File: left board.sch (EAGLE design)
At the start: 29 parts, among them IC1 LM555D, IC2 LM555D

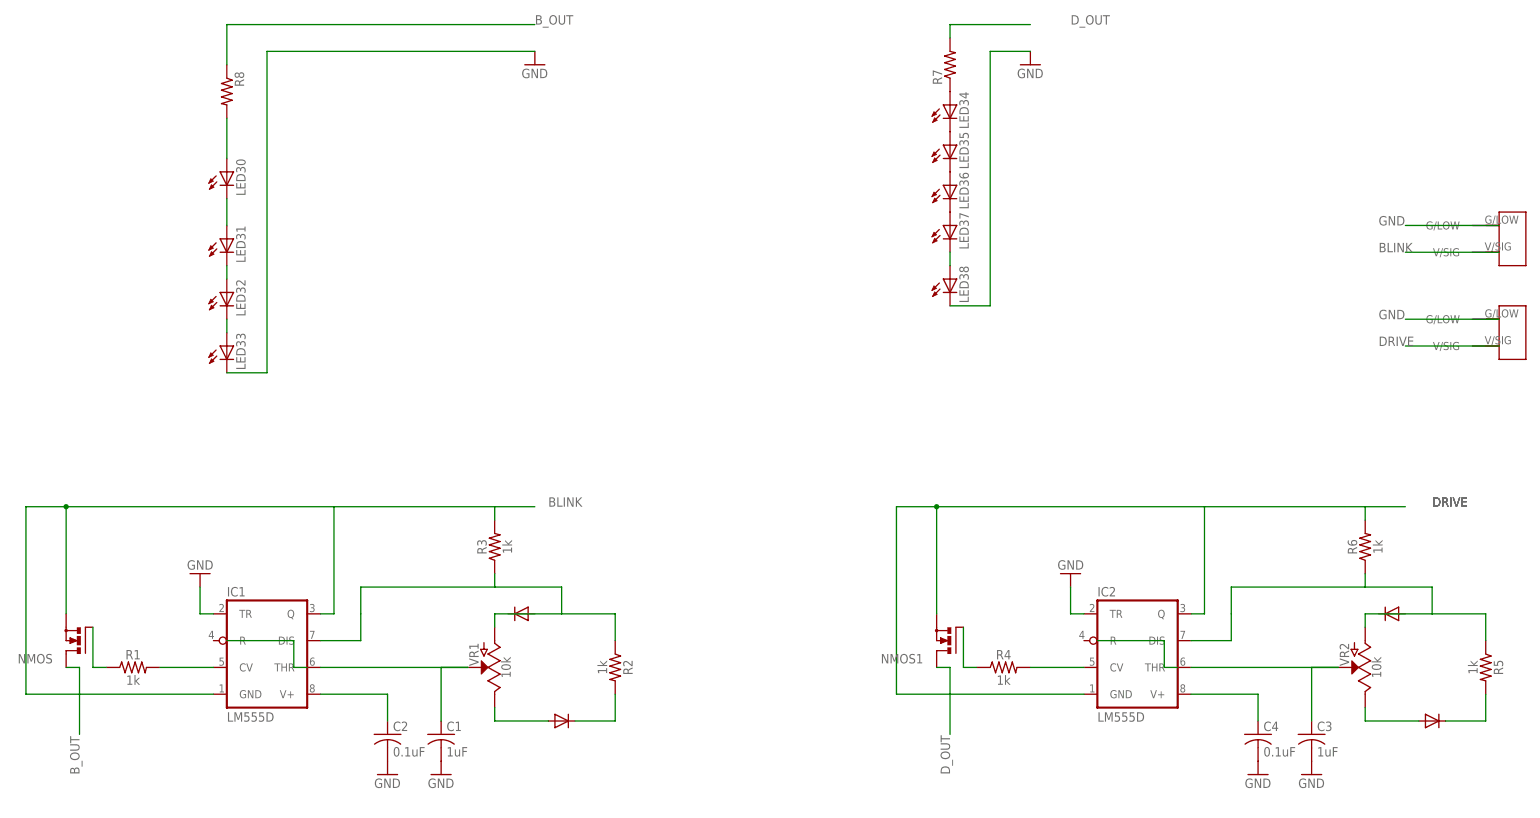
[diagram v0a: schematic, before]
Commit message: added switches to light board
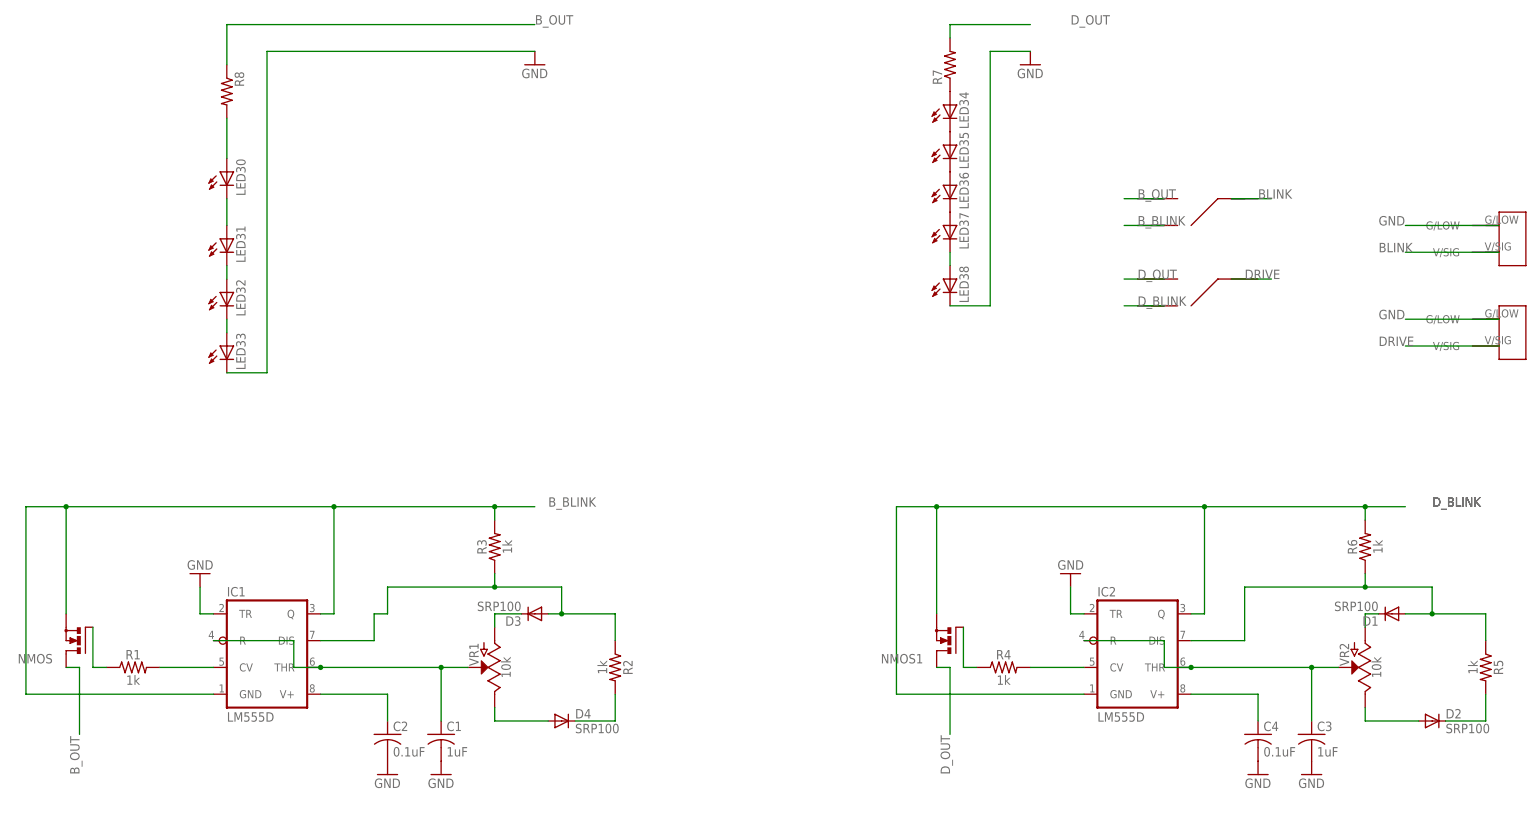
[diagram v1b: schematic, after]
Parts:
- added D1, D2, D3, D4: SRP100, diode:SRP100
- added U$1, U$2: JS_SERIES_SLIDESWITCCH, slide switch:JS_SERIES_SLIDESWITCCH
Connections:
- removed net N$12: IC2.DIS
- new net B_BLINK: IC1.GND, IC1.Q, NMOS.S, R3.2, U$1.OUT1
- new net D_BLINK: IC2.GND, IC2.Q, NMOS1.S, R6.2, U$2.OUT1
- new net N$9: D1.C, VR2.A
- net BLINK: now also U$1.IN; no longer IC1.GND, IC1.Q, NMOS.S, R3.2
- net B_OUT: now also U$1.OUT2
- net DRIVE: now also U$2.IN; no longer IC2.GND, IC2.Q, NMOS1.S, R6.2
- net D_OUT: now also U$2.OUT2
- net N$13: now also IC2.R
- net N$14: now also D1.A, IC2.DIS; no longer VR2.A
- net N$17: now also D2.A
- net N$18: now also D2.C
- net N$2: now also D3.C, VR1.A; no longer IC1.DIS
- net N$3: now also IC1.R
- net N$4: now also D3.A, IC1.DIS; no longer VR1.A
- net N$5: now also D4.A
- net N$7: now also D4.C

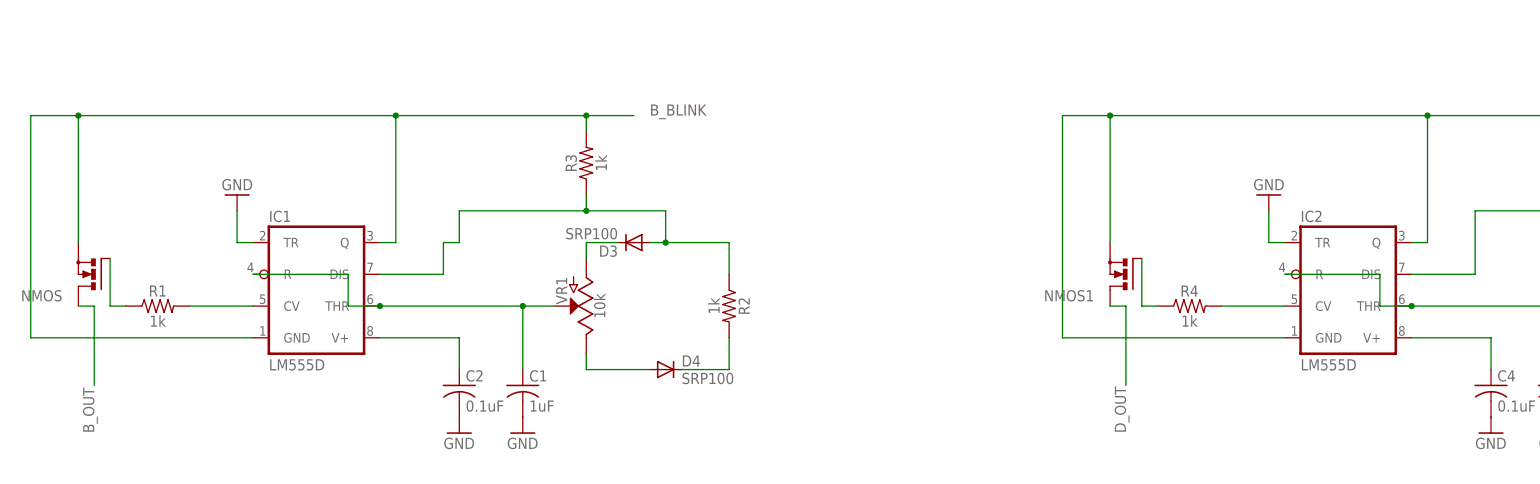
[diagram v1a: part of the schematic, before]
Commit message: updated for correct fets and routing
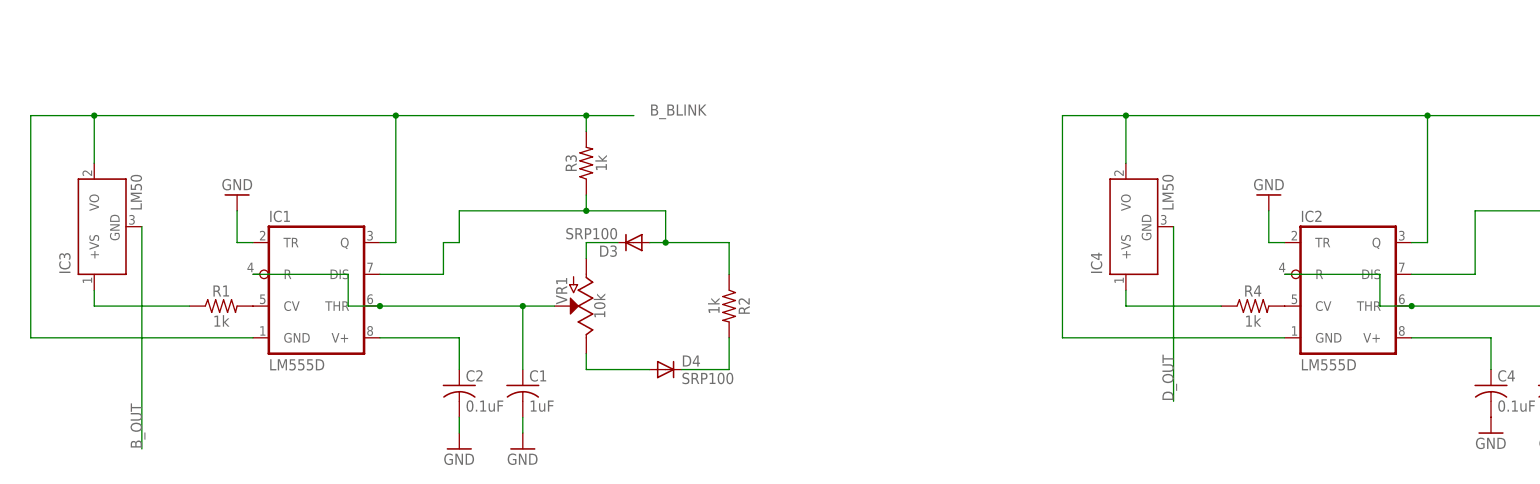
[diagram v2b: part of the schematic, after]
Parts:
- removed NMOS, NMOS1: (no value), transistor-power:N-MOSFET-SO8S
- added IC3, IC4: LM50, linear:LM50
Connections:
- removed net N$19: NMOS1.G, R4.1
- removed net N$8: NMOS.G, R1.1
- new net N$1: IC3.+VS, R1.1
- new net N$11: IC4.+VS, R4.1
- net B_BLINK: now also IC3.VO; no longer NMOS.S
- net B_OUT: now also IC3.GND; no longer NMOS.D
- net D_BLINK: now also IC4.VO; no longer NMOS1.S
- net D_OUT: now also IC4.GND; no longer NMOS1.D
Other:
- moved on the sheet: R1, R4
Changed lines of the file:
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@@
 <part name="C2" library="E-P-008-R1.2" deviceset="C-US" device="025-024X044" value="0.1uF"/>
 <part name="GND1" library="E-P-008-R1.2" deviceset="GND" device=""/>
-<part name="NMOS" library="transistor-power" library_urn="urn:adsk.eagle:library:400" deviceset="N-MOSFET-SO8" device="S" package3d_urn="urn:adsk.eagle:package:29505/2"/>
 <part name="GND2" library="E-P-008-R1.2" deviceset="GND" device=""/>
 <part name="GND4" library="E-P-008-R1.2" deviceset="GND" device=""/>
@@
 <part name="C4" library="E-P-008-R1.2" deviceset="C-US" device="025-024X044" value="0.1uF"/>
 <part name="GND5" library="E-P-008-R1.2" deviceset="GND" device=""/>
-<part name="NMOS1" library="transistor-power" library_urn="urn:adsk.eagle:library:400" deviceset="N-MOSFET-SO8" device="S" package3d_urn="urn:adsk.eagle:package:29505/2"/>
 <part name="GND6" library="E-P-008-R1.2" deviceset="GND" device=""/>
 <part name="GND8" library="E-P-008-R1.2" deviceset="GND" device=""/>
@@
 <part name="D3" library="diode" library_urn="urn:adsk.eagle:library:210" deviceset="SRP100" device="" package3d_urn="urn:adsk.eagle:package:43336/1"/>
 <part name="D4" library="diode" library_urn="urn:adsk.eagle:library:210" deviceset="SRP100" device="" package3d_urn="urn:adsk.eagle:package:43336/1"/>
+<part name="IC3" library="linear" library_urn="urn:adsk.eagle:library:262" deviceset="LM50" device="" package3d_urn="urn:adsk.eagle:package:16489/1"/>
+<part name="IC4" library="linear" library_urn="urn:adsk.eagle:library:262" deviceset="LM50" device="" package3d_urn="urn:adsk.eagle:package:16489/1"/>
 </parts>
 <sheets>
@@
 <instance part="L_BLINK" gate="G$1" x="157.48" y="63.5"/>
 <instance part="IC1" gate="A" x="-81.28" y="-15.24"/>
-<instance part="R1" gate="G$1" x="-106.68" y="-17.78"/>
+<instance part="R1" gate="G$1" x="-96.52" y="-17.78"/>
 <instance part="R2" gate="G$1" x="-15.24" y="-17.78" rot="R270"/>
 <instance part="R3" gate="G$1" x="-38.1" y="5.08" rot="R90"/>
@@
 <instance part="C1" gate="G$1" x="-48.26" y="-30.48"/>
 <instance part="C2" gate="G$1" x="-58.42" y="-30.48"/>
-<instance part="GND1" gate="1" x="-48.26" y="-38.1"/>
-<instance part="NMOS" gate="G$1" x="-116.84" y="-12.7" rot="R180"/>
-<instance part="GND2" gate="1" x="-58.42" y="-38.1"/>
+<instance part="GND1" gate="1" x="-48.26" y="-40.64"/>
+<instance part="GND2" gate="1" x="-58.42" y="-40.64"/>
 <instance part="GND4" gate="1" x="-93.98" y="0" rot="R180"/>
 <instance part="IC2" gate="A" x="83.82" y="-15.24"/>
-<instance part="R4" gate="G$1" x="58.42" y="-17.78"/>
+<instance part="R4" gate="G$1" x="68.58" y="-17.78"/>
 <instance part="R5" gate="G$1" x="149.86" y="-17.78" rot="R270"/>
 <instance part="R6" gate="G$1" x="127" y="5.08" rot="R90"/>
@@
 <instance part="C4" gate="G$1" x="106.68" y="-30.48"/>
 <instance part="GND5" gate="1" x="116.84" y="-38.1"/>
-<instance part="NMOS1" gate="G$1" x="48.26" y="-12.7" rot="R180"/>
 <instance part="GND6" gate="1" x="106.68" y="-38.1"/>
 <instance part="GND8" gate="1" x="71.12" y="0" rot="R180"/>
@@
 <instance part="D3" gate="1" x="-30.48" y="-7.62" rot="R180"/>
 <instance part="D4" gate="1" x="-25.4" y="-27.94"/>
+<instance part="IC3" gate="G$1" x="-116.84" y="-5.08" rot="R90"/>
+<instance part="IC4" gate="G$1" x="48.26" y="-5.08" rot="R90"/>
 </instances>
 <busses>
@@
 <pinref part="GND2" gate="1" pin="GND"/>
 <pinref part="C2" gate="G$1" pin="2"/>
+<wire x1="-58.42" y1="-38.1" x2="-58.42" y2="-35.56" width="0.1524" layer="91"/>
 </segment>
 <segment>
 <pinref part="GND1" gate="1" pin="GND"/>
 <pinref part="C1" gate="G$1" pin="2"/>
+<wire x1="-48.26" y1="-38.1" x2="-48.26" y2="-35.56" width="0.1524" layer="91"/>
 </segment>
 <segment>
@@
 <pinref part="IC1" gate="A" pin="CV"/>
 <pinref part="R1" gate="G$1" pin="2"/>
-<wire x1="-91.44" y1="-17.78" x2="-101.6" y2="-17.78" width="0.1524" layer="91"/>
 </segment>
 </net>
@@
 <pinref part="D4" gate="1" pin="C"/>
 <wire x1="-22.86" y1="-27.94" x2="-15.24" y2="-27.94" width="0.1524" layer="91"/>
-</segment>
-</net>
-<net name="N$8" class="0">
-<segment>
-<pinref part="R1" gate="G$1" pin="1"/>
-<pinref part="NMOS" gate="G$1" pin="G"/>
-<wire x1="-111.76" y1="-17.78" x2="-114.3" y2="-17.78" width="0.1524" layer="91"/>
-<wire x1="-114.3" y1="-17.78" x2="-114.3" y2="-10.16" width="0.1524" layer="91"/>
 </segment>
 </net>
@@
 <pinref part="IC2" gate="A" pin="CV"/>
 <pinref part="R4" gate="G$1" pin="2"/>
-<wire x1="73.66" y1="-17.78" x2="63.5" y2="-17.78" width="0.1524" layer="91"/>
 </segment>
 </net>
@@
 </segment>
 </net>
-<net name="N$19" class="0">
-<segment>
-<pinref part="R4" gate="G$1" pin="1"/>
-<pinref part="NMOS1" gate="G$1" pin="G"/>
-<wire x1="53.34" y1="-17.78" x2="50.8" y2="-17.78" width="0.1524" layer="91"/>
-<wire x1="50.8" y1="-17.78" x2="50.8" y2="-10.16" width="0.1524" layer="91"/>
-</segment>
-</net>
 <net name="BLINK" class="0">
 <segment>
@@
 </segment>
 <segment>
-<pinref part="NMOS" gate="G$1" pin="D"/>
-<wire x1="-119.38" y1="-17.78" x2="-116.84" y2="-17.78" width="0.1524" layer="91"/>
-<wire x1="-116.84" y1="-17.78" x2="-116.84" y2="-30.48" width="0.1524" layer="91"/>
-<label x="-116.84" y="-38.1" size="1.778" layer="95" rot="R90"/>
-</segment>
-<segment>
 <pinref part="U$1" gate="G$1" pin="OUT2"/>
 <wire x1="88.9" y1="71.12" x2="81.28" y2="71.12" width="0.1524" layer="91"/>
 <label x="83.82" y="71.12" size="1.778" layer="95"/>
+</segment>
+<segment>
+<wire x1="-109.22" y1="-5.08" x2="-109.22" y2="-40.64" width="0.1524" layer="91"/>
+<label x="-109.22" y="-40.64" size="1.778" layer="95" rot="R90"/>
+<pinref part="IC3" gate="G$1" pin="GND"/>
 </segment>
 </net>
@@
 </segment>
 <segment>
-<pinref part="NMOS1" gate="G$1" pin="D"/>
-<wire x1="45.72" y1="-17.78" x2="48.26" y2="-17.78" width="0.1524" layer="91"/>
-<wire x1="48.26" y1="-17.78" x2="48.26" y2="-30.48" width="0.1524" layer="91"/>
-<label x="48.26" y="-38.1" size="1.778" layer="95" rot="R90"/>
-</segment>
-<segment>
 <pinref part="U$2" gate="G$1" pin="OUT2"/>
 <wire x1="88.9" y1="55.88" x2="81.28" y2="55.88" width="0.1524" layer="91"/>
 <label x="83.82" y="55.88" size="1.778" layer="95"/>
 </segment>
+<segment>
+<pinref part="IC4" gate="G$1" pin="GND"/>
+<wire x1="55.88" y1="-5.08" x2="55.88" y2="-33.02" width="0.1524" layer="91"/>
+<label x="55.88" y="-33.02" size="1.778" layer="95" rot="R90"/>
+</segment>
 </net>
 <net name="D_BLINK" class="0">
@@
 <segment>
 <pinref part="IC2" gate="A" pin="GND"/>
-<wire x1="38.1" y1="12.7" x2="45.72" y2="12.7" width="0.1524" layer="91"/>
-<wire x1="45.72" y1="12.7" x2="96.52" y2="12.7" width="0.1524" layer="91"/>
+<wire x1="38.1" y1="12.7" x2="48.26" y2="12.7" width="0.1524" layer="91"/>
+<wire x1="48.26" y1="12.7" x2="96.52" y2="12.7" width="0.1524" layer="91"/>
 <wire x1="96.52" y1="12.7" x2="127" y2="12.7" width="0.1524" layer="91"/>
 <wire x1="127" y1="12.7" x2="134.62" y2="12.7" width="0.1524" layer="91"/>
 <wire x1="73.66" y1="-22.86" x2="38.1" y2="-22.86" width="0.1524" layer="91"/>
 <wire x1="38.1" y1="-22.86" x2="38.1" y2="12.7" width="0.1524" layer="91"/>
-<pinref part="NMOS1" gate="G$1" pin="S"/>
-<wire x1="45.72" y1="-7.62" x2="45.72" y2="12.7" width="0.1524" layer="91"/>
-<junction x="45.72" y="12.7"/>
 <label x="139.7" y="12.7" size="1.778" layer="95"/>
 <label x="139.7" y="12.7" size="1.778" layer="95"/>
@@
 <wire x1="127" y1="10.16" x2="127" y2="12.7" width="0.1524" layer="91"/>
 <junction x="127" y="12.7"/>
+<pinref part="IC4" gate="G$1" pin="VO"/>
+<wire x1="48.26" y1="5.08" x2="48.26" y2="12.7" width="0.1524" layer="91"/>
+<junction x="48.26" y="12.7"/>
 </segment>
 </net>
@@
 <segment>
 <pinref part="IC1" gate="A" pin="GND"/>
-<wire x1="-127" y1="12.7" x2="-119.38" y2="12.7" width="0.1524" layer="91"/>
-<wire x1="-119.38" y1="12.7" x2="-68.58" y2="12.7" width="0.1524" layer="91"/>
+<wire x1="-127" y1="12.7" x2="-116.84" y2="12.7" width="0.1524" layer="91"/>
+<wire x1="-116.84" y1="12.7" x2="-68.58" y2="12.7" width="0.1524" layer="91"/>
 <wire x1="-68.58" y1="12.7" x2="-38.1" y2="12.7" width="0.1524" layer="91"/>
 <wire x1="-38.1" y1="12.7" x2="-30.48" y2="12.7" width="0.1524" layer="91"/>
 <wire x1="-91.44" y1="-22.86" x2="-127" y2="-22.86" width="0.1524" layer="91"/>
 <wire x1="-127" y1="-22.86" x2="-127" y2="12.7" width="0.1524" layer="91"/>
-<pinref part="NMOS" gate="G$1" pin="S"/>
-<wire x1="-119.38" y1="-7.62" x2="-119.38" y2="12.7" width="0.1524" layer="91"/>
-<junction x="-119.38" y="12.7"/>
 <label x="-27.94" y="12.7" size="1.778" layer="95"/>
 <pinref part="IC1" gate="A" pin="Q"/>
@@
 <wire x1="-38.1" y1="10.16" x2="-38.1" y2="12.7" width="0.1524" layer="91"/>
 <junction x="-38.1" y="12.7"/>
+<pinref part="IC3" gate="G$1" pin="VO"/>
+<wire x1="-116.84" y1="5.08" x2="-116.84" y2="12.7" width="0.1524" layer="91"/>
+<junction x="-116.84" y="12.7"/>
 </segment>
 </net>
@@
 </segment>
 </net>
+<net name="N$11" class="0">
+<segment>
+<pinref part="R4" gate="G$1" pin="1"/>
+<pinref part="IC4" gate="G$1" pin="+VS"/>
+<wire x1="48.26" y1="-15.24" x2="48.26" y2="-17.78" width="0.1524" layer="91"/>
+<wire x1="48.26" y1="-17.78" x2="63.5" y2="-17.78" width="0.1524" layer="91"/>
+</segment>
+</net>
+<net name="N$1" class="0">
+<segment>
+<pinref part="IC3" gate="G$1" pin="+VS"/>
+<pinref part="R1" gate="G$1" pin="1"/>
+<wire x1="-116.84" y1="-15.24" x2="-116.84" y2="-17.78" width="0.1524" layer="91"/>
+<wire x1="-116.84" y1="-17.78" x2="-101.6" y2="-17.78" width="0.1524" layer="91"/>
+</segment>
+</net>

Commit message: Gerbers generated
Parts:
- removed C2, C4: 0.1uF, E-P-008-R1.2:C-US025-024X044
- removed D1, D2, D3, D4: SRP100, diode:SRP100
- removed IC3, IC4: LM50, linear:LM50
- removed LED30, LED31, LED32, LED33, LED34, LED35, LED36, LED37, LED38: (no value), E-P-008-R1.2:LED
- removed R1, R2, R3, R4, R5, R6: 1k, SparkFun-Resistors:1KOHM-0603-1/10W-1%
- removed VR1, VR2: 10k, SparkFun-Resistors:POTENTIOMETER-PTH-9MM-1/20W-20%
- added C5, C6: 1.0uF, SparkFun-Capacitors-extra:1.0UF-25V-+80/-20(0805)"
- added D10, D11, D12, D13, D14, D15, D16, D17, D18, D19, D20, D21, D22, D23, D24, D25, D26, D27, D28, D5, D6, D7, D8, D9: (no value), SparkFun-LED:LED5MM
- added D29, D30, D31, D32: (no value), SparkFun-DiscreteSemi:DIODESMA
- added Q1, Q2: 10, transistor-power:PMOSFET_NTO220BV
- added R10, R11, R14, R9: 1k, SparkFun-Resistors:0.22OHM-1/4W-1%(0805)
- added R12, R13: 30, SparkFun-Resistors:0.22OHM-1/4W-1%(0805)
- added U$3, U$4: 10K_LINEAR_POT_SMD, SparkFun-Resistors:10K_LINEAR_POT_SMD
- C1, C3: value 1uF -> 0.1uF; device E-P-008-R1.2:C-US025-024X044 -> SparkFun-Capacitors-extra:0.1UF-25V(+80/-20%)(0603)
- R7: value (none) -> 1k; device resistor:R-US_0204/2V -> SparkFun-Resistors:0.22OHM-1/4W-1%(0805)
- R8: value (none) -> 1k; device resistor:R-US_0204/5 -> SparkFun-Resistors:0.22OHM-1/4W-1%(0805)
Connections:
- removed net N$37: LED30.C, LED31.A
- removed net N$38: LED31.C, LED32.A
- removed net N$39: LED32.C, LED33.A
- removed net N$40: LED34.C, LED35.A
- removed net N$41: LED35.C, LED36.A
- removed net N$42: LED36.C, LED37.A
- removed net N$43: LED30.A, R8.2
- removed net N$44: LED34.A, R7.1
- removed net N$48: LED37.C, LED38.A
- new net N$12: D10.A, D11.A, D12.A, D5.C, D6.C, D7.C, D8.C, D9.A
- new net N$19: D17.A, D18.A, D19.A, D20.A, R13.1
- new net N$21: D10.C, D11.C, D12.C, D13.A, D14.A, D15.A, D16.A, D9.C
- new net N$22: D21.C, D22.C, D23.C, D24.C, D25.A, D26.A, D27.A, D28.A
- new net N$23: D17.C, D18.C, D19.C, D20.C, D21.A, D22.A, D23.A, D24.A
- new net N$8: IC2.CV, R14.2
- net B_BLINK: now also Q2.S, R9.2; no longer IC3.VO, R3.2
- net B_OUT: now also Q2.G, R12.1; no longer IC3.GND, R8.1
- net D_BLINK: now also Q1.S, R8.2; no longer IC4.VO, R6.2
- net D_OUT: now also Q1.G, R13.2; no longer IC4.GND, R7.2
- net GND: now also C5.2, C6.2, D13.C, D14.C, D15.C, D16.C, D25.C, D26.C, D27.C, D28.C; no longer C2.2, C4.2, LED33.C, LED38.C
- net N$1: now also Q2.D, R11.2; no longer IC3.+VS, R1.1
- net N$10: now also R11.1; no longer R1.2
- net N$11: now also Q1.D, R14.1; no longer IC4.+VS, R4.1
- net N$13: now also C5.1, U$4.S; no longer C3.1, VR2.S
- net N$14: now also D30.A, R7.2, R8.1; no longer D1.A, R5.1, R6.1
- net N$15: now also C3.1; no longer C4.1
- net N$16: now also D5.A, D6.A, D7.A, D8.A, R12.2; no longer IC2.CV, R4.2
- net N$17: now also D29.A, U$4.E; no longer D2.A, VR2.E
- net N$18: now also D29.C, R7.1; no longer D2.C, R5.2
- net N$2: now also D32.C, U$3.A; no longer D3.C, VR1.A
- net N$3: now also C6.1, U$3.S; no longer C1.1, VR1.S
- net N$4: now also D32.A, R10.2, R9.1; no longer D3.A, R2.1, R3.1
- net N$5: now also D31.A, U$3.E; no longer D4.A, VR1.E
- net N$6: now also C1.1; no longer C2.1
- net N$7: now also D31.C, R10.1; no longer D4.C, R2.2
- net N$9: now also D30.C, U$4.A; no longer D1.C, VR2.A
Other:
- moved on the sheet: R7, R8
